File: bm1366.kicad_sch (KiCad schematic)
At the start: 21 parts, among them J2 Conn_01x06, U20 TMP451A, U21 TMUX1109RSVR, U22 TMP451J, U23 TMUX1109RSVR, U35 TXU0304PW, U8 25MHz

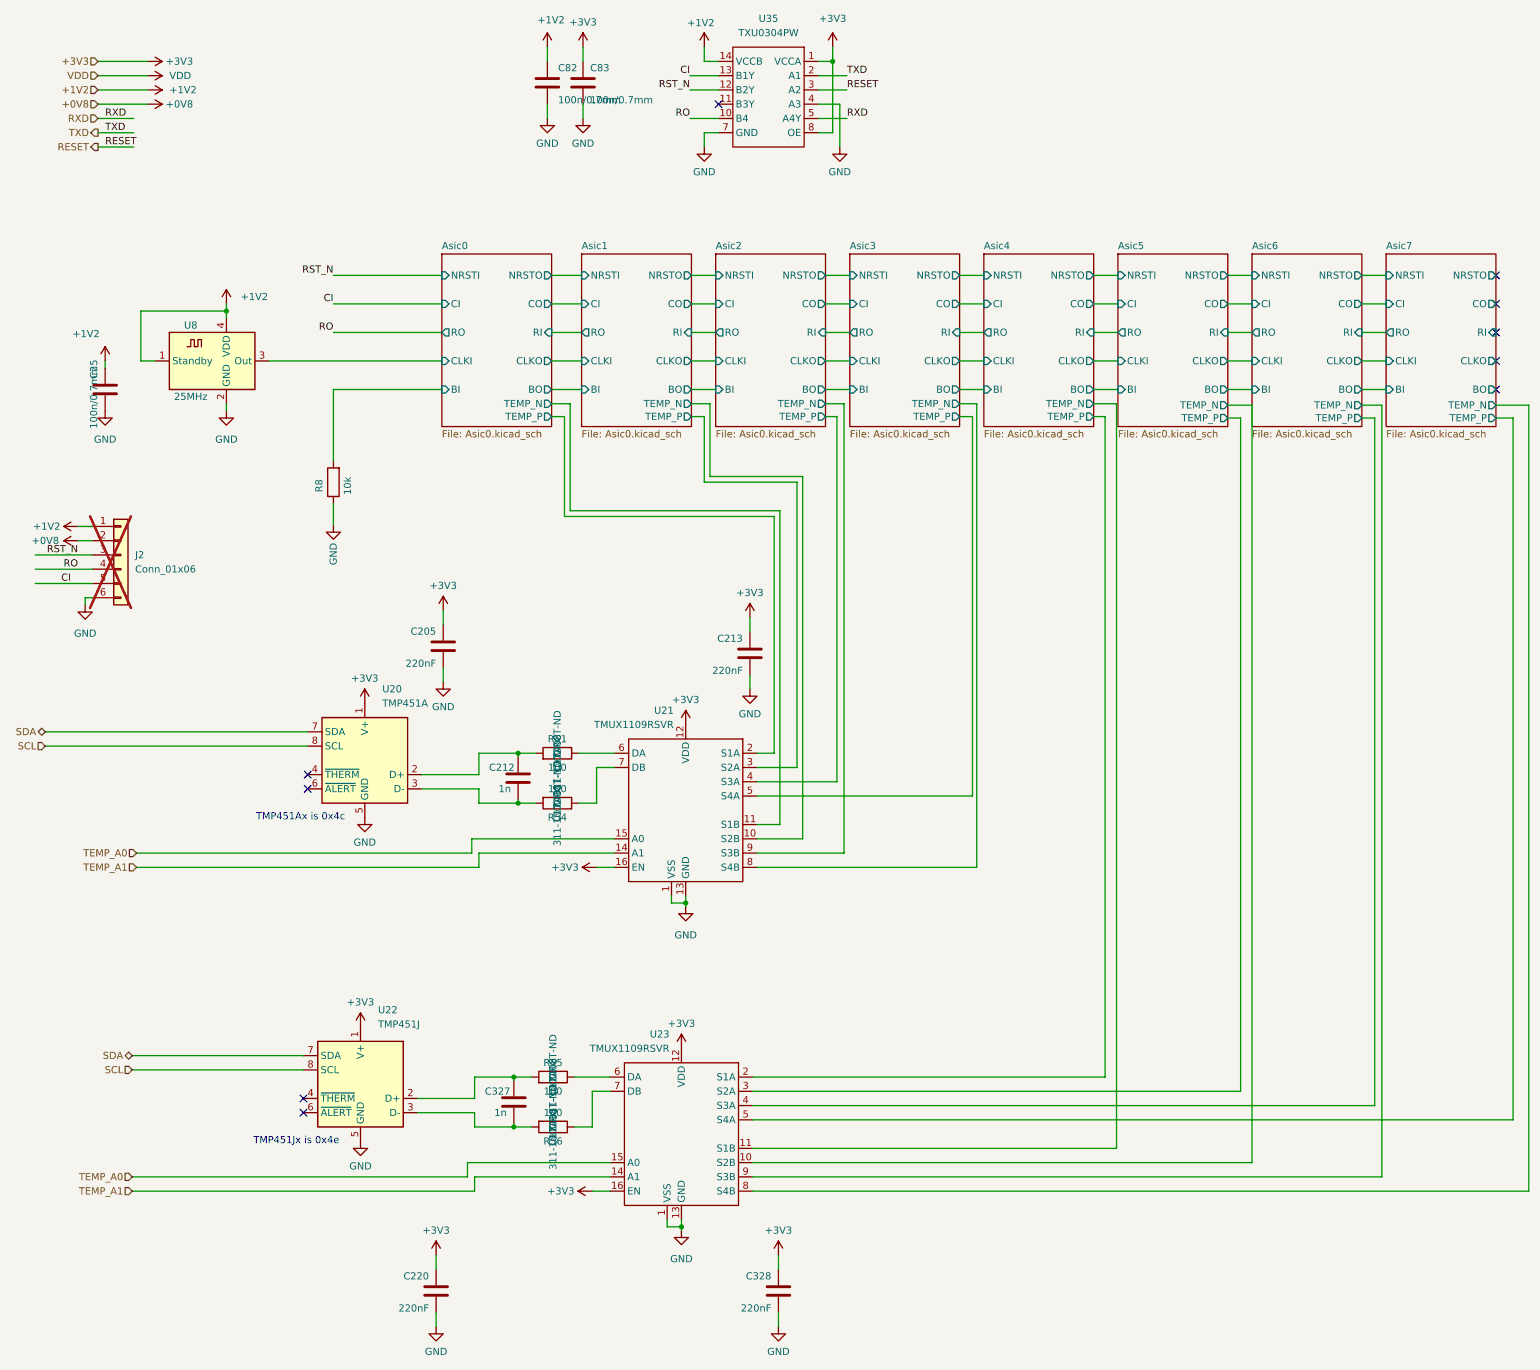
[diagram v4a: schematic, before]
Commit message: Tmux Variant
- Added curcuit to read internal Asictemps per chip
- (i)BOM changes
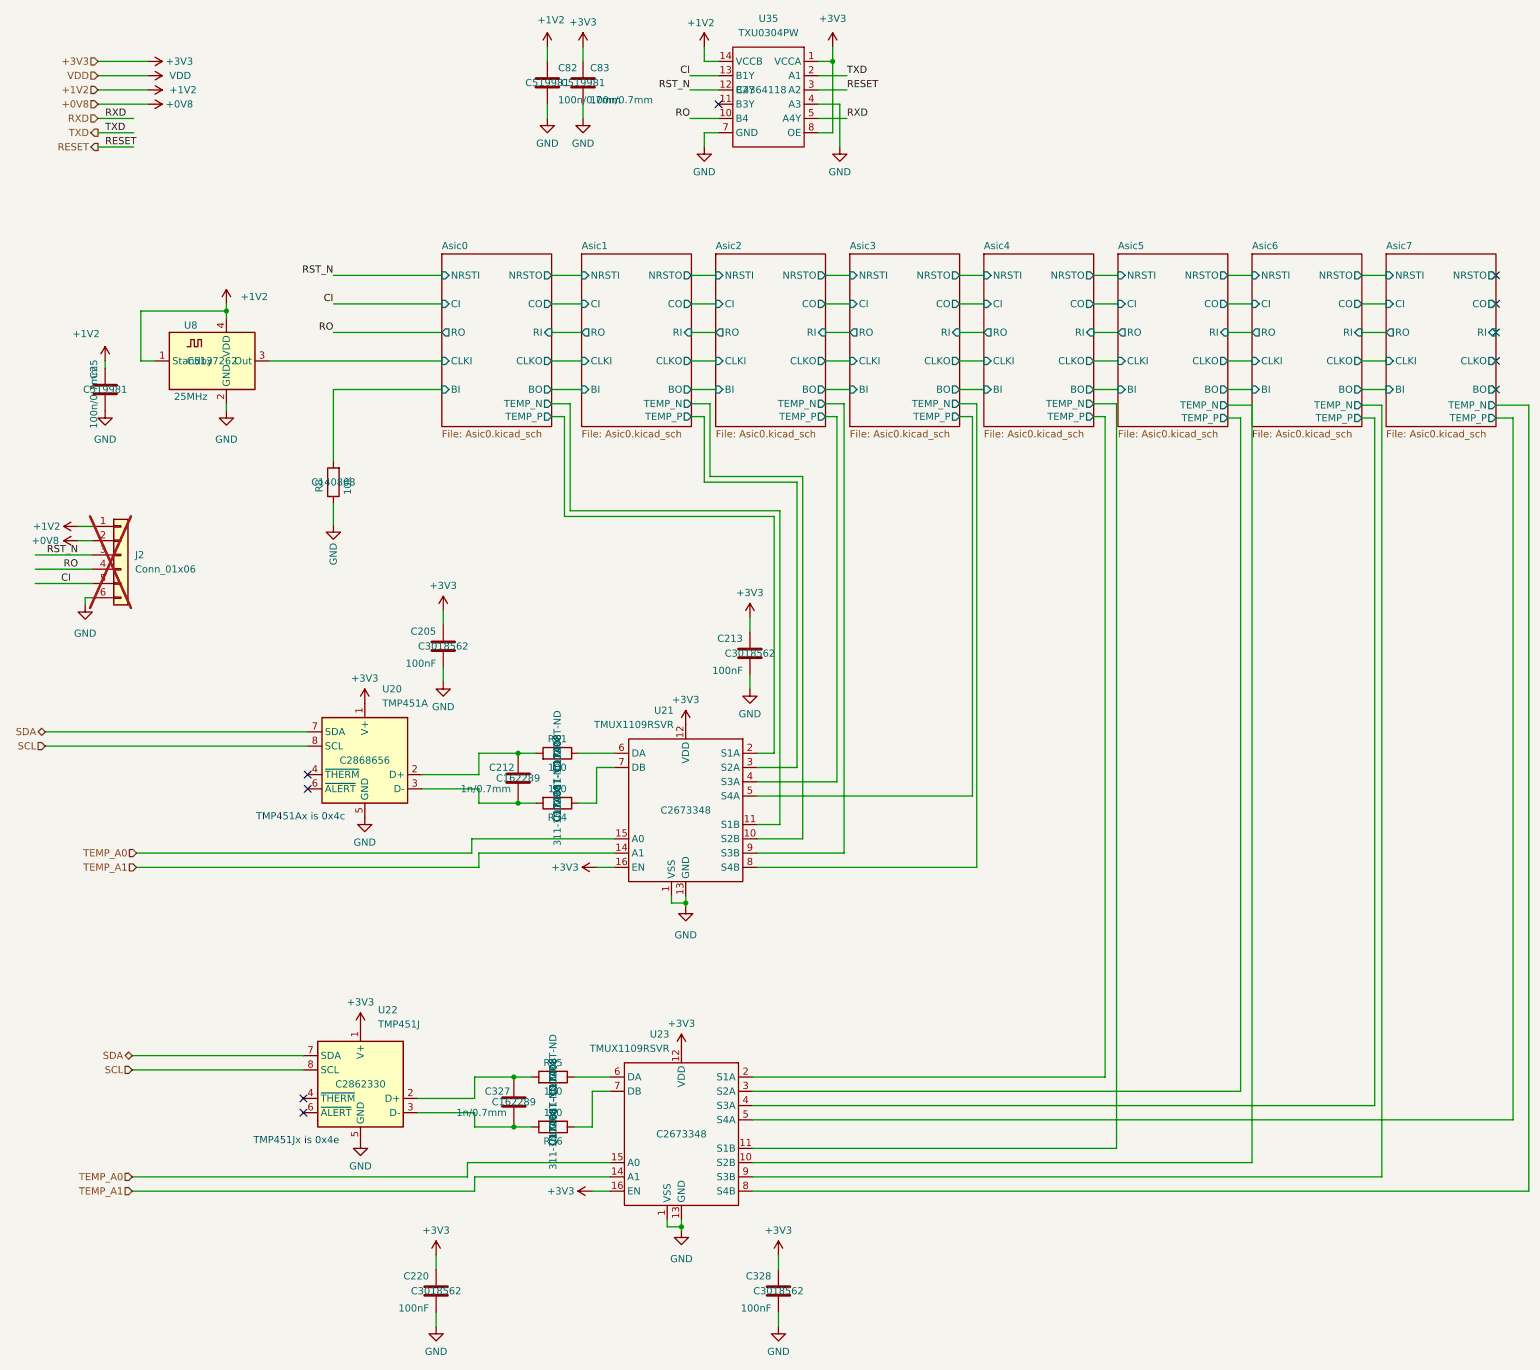
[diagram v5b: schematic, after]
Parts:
- C205, C213, C220, C328: value 220nF -> 100nF; LCSC Part # (none) -> C3018562
- C212, C327: value 1n -> 1n/0.7mm; LCSC Part # (none) -> C162289; Manufacturer C0805C102K2GECAUTO -> GRM2165C2A102JA01D; OrderNr 399-17171-1-ND -> 490-6445-1-ND
- C25, C82, C83: LCSC Part # (none) -> C519981
- R51, R54, R55, R56: LCSC Part # (none) -> C17408
- R8: LCSC Part # (none) -> C140868
- U20: LCSC Part # (none) -> C2868656
- U21, U23: LCSC Part # (none) -> C2673348
- U22: LCSC Part # (none) -> C2862330
- U35: LCSC Part # (none) -> C4364118
- U8: LCSC Part # (none) -> C5137262
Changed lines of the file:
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@@
 			)
 		)
+		(property "LCSC Part #" "C2673348"
+			(at 133.858 165.1 0)
+			(effects
+				(font
+					(size 1.27 1.27)
+				)
+			)
+		)
 		(pin "8"
 		)
@@
 			)
 		)
+		(property "LCSC Part #" "C4364118"
+			(at 147.32 36.83 0)
+			(effects
+				(font
+					(size 1.27 1.27)
+				)
+			)
+		)
 		(pin "8"
 		)
@@
 			)
 		)
-		(property "Value" "220nF"
+		(property "Value" "100nF"
 			(at 88.138 254.508 0)
 			(effects
@@
 			)
 		)
+		(property "LCSC Part #" "C3018562"
+			(at 89.408 250.698 0)
+			(effects
+				(font
+					(size 1.27 1.27)
+				)
+			)
+		)
 		(pin "1"
 		)
@@
 			)
 		)
+		(property "LCSC Part #" "C519981"
+			(at 115.57 35.56 0)
+			(effects
+				(font
+					(size 1.27 1.27)
+				)
+			)
+		)
 		(pin "1"
 		)
@@
 			)
 		)
+		(property "LCSC Part #" "C2673348"
+			(at 133.096 222.758 0)
+			(effects
+				(font
+					(size 1.27 1.27)
+				)
+			)
+		)
 		(pin "8"
 		)
@@
 			)
 		)
+		(property "LCSC Part #" "C2868656"
+			(at 76.708 156.21 0)
+			(effects
+				(font
+					(size 1.27 1.27)
+				)
+			)
+		)
 		(pin "1"
 		)
@@
 			)
 		)
+		(property "LCSC Part #" "C519981"
+			(at 30.48 90.17 0)
+			(effects
+				(font
+					(size 1.27 1.27)
+				)
+			)
+		)
 		(pin "1"
 		)
@@
 			)
 		)
+		(property "LCSC Part #" "C17408"
+			(at 110.998 163.83 0)
+			(effects
+				(font
+					(size 1.27 1.27)
+				)
+			)
+		)
 		(pin "1"
 		)
@@
 			)
 		)
-		(property "Value" "220nF"
+		(property "Value" "100nF"
 			(at 144.018 140.97 0)
 			(effects
@@
 			)
 		)
+		(property "LCSC Part #" "C3018562"
+			(at 145.288 137.16 0)
+			(effects
+				(font
+					(size 1.27 1.27)
+				)
+			)
+		)
 		(pin "1"
 		)
@@
 			)
 		)
+		(property "LCSC Part #" "C17408"
+			(at 110.236 212.598 0)
+			(effects
+				(font
+					(size 1.27 1.27)
+				)
+			)
+		)
 		(pin "1"
 		)
@@
 			)
 		)
-		(property "Value" "220nF"
+		(property "Value" "100nF"
 			(at 149.098 254.508 0)
 			(effects
@@
 			)
 		)
+		(property "LCSC Part #" "C3018562"
+			(at 150.368 250.698 0)
+			(effects
+				(font
+					(size 1.27 1.27)
+				)
+			)
+		)
 		(pin "1"
 		)
@@
 			)
 		)
-		(property "Value" "220nF"
+		(property "Value" "100nF"
 			(at 89.408 139.7 0)
 			(effects
@@
 			)
 		)
+		(property "LCSC Part #" "C3018562"
+			(at 90.678 135.89 0)
+			(effects
+				(font
+					(size 1.27 1.27)
+				)
+			)
+		)
 		(pin "1"
 		)
@@
 			)
 		)
+		(property "LCSC Part #" "C17408"
+			(at 110.998 154.94 0)
+			(effects
+				(font
+					(size 1.27 1.27)
+				)
+			)
+		)
 		(pin "1"
 		)
@@
 			)
 		)
+		(property "LCSC Part #" "C5137262"
+			(at 49.53 85.09 0)
+			(effects
+				(font
+					(size 1.27 1.27)
+				)
+			)
+		)
 		(pin "1"
 		)
@@
 			)
 		)
+		(property "LCSC Part #" "C140868"
+			(at 71.12 106.68 0)
+			(effects
+				(font
+					(size 1.27 1.27)
+				)
+			)
+		)
 		(pin "1"
 		)
@@
 			)
 		)
+		(property "LCSC Part #" "C519981"
+			(at 109.22 35.56 0)
+			(effects
+				(font
+					(size 1.27 1.27)
+				)
+			)
+		)
 		(pin "1"
 		)
@@
 			)
 		)
+		(property "LCSC Part #" "C17408"
+			(at 110.236 221.488 0)
+			(effects
+				(font
+					(size 1.27 1.27)
+				)
+			)
+		)
 		(pin "1"
 		)
@@
 			)
 		)
-		(property "Value" "1n"
+		(property "Value" "1n/0.7mm"
 			(at 101.981 218.948 0)
 			(effects
@@
 			)
 		)
-		(property "Manufacturer" "C0805C102K2GECAUTO"
+		(property "Manufacturer" "GRM2165C2A102JA01D"
 			(at 103.251 217.043 0)
 			(effects
@@
 			)
 		)
-		(property "OrderNr" "399-17171-1-ND"
+		(property "OrderNr" "490-6445-1-ND"
 			(at 103.251 217.043 0)
 			(effects
@@
 			)
 		)
+		(property "LCSC Part #" "C162289"
+			(at 103.251 217.043 0)
+			(effects
+				(font
+					(size 1.27 1.27)
+				)
+			)
+		)
 		(pin "1"
 		)
@@
 			)
 		)
+		(property "LCSC Part #" "C2862330"
+			(at 75.946 213.868 0)
+			(effects
+				(font
+					(size 1.27 1.27)
+				)
+			)
+		)
 		(pin "1"
 		)
@@
 			)
 		)
-		(property "Value" "1n"
+		(property "Value" "1n/0.7mm"
 			(at 102.743 161.29 0)
 			(effects
@@
 			)
 		)
-		(property "Manufacturer" "C0805C102K2GECAUTO"
+		(property "Manufacturer" "GRM2165C2A102JA01D"
 			(at 104.013 159.385 0)
 			(effects
@@
 			)
 		)
-		(property "OrderNr" "399-17171-1-ND"
+		(property "OrderNr" "490-6445-1-ND"
 			(at 104.013 159.385 0)
 			(effects
@@
 			)
 		)
+		(property "LCSC Part #" "C162289"
+			(at 104.013 159.385 0)
+			(effects
+				(font
+					(size 1.27 1.27)
+				)
+			)
+		)
 		(pin "1"
 		)
@@
 			)
 		)
+		(property "LCSC Part #" ""
+			(at 33.274 119.634 0)
+			(effects
+				(font
+					(size 1.27 1.27)
+				)
+			)
+		)
